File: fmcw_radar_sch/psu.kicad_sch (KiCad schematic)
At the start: 0 parts

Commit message: added MCU PSU VCO
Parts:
- added C1: 100nF, Capacitor_SMD:C_1206_3216Metric_Pad1.33x1.80mm_HandSolder, symbol Device:C_Small
- added C2: 10uF, Capacitor_SMD:C_1206_3216Metric_Pad1.33x1.80mm_HandSolder, symbol Device:C_Small
- added C203: 100n, Capacitor_SMD:C_0603_1608Metric, symbol Device:C
- added C205, C208: 1u, Capacitor_SMD:C_0805_2012Metric, symbol Device:C
- added C212, C215: 22u, Capacitor_SMD:C_0805_2012Metric, symbol Device:C
- added C3, C4: 22uF, Capacitor_SMD:C_1206_3216Metric_Pad1.33x1.80mm_HandSolder, symbol Device:C_Small
- added D204, D306, D307: Green, LED_SMD:LED_0603_1608Metric_Pad1.05x0.95mm_HandSolder, symbol Device:LED
- added J1: USB_B, Connector_USB:USB_B_OST_USB-B1HSxx_Horizontal, symbol Connector:USB_B
- added J2: Screw_Terminal_01x02, TerminalBlock:TerminalBlock_MaiXu_MX126-5.0-02P_1x02_P5.00mm, symbol Connector:Screw_Terminal_01x02
- added L1: 3.9uH, Inductor_SMD:L_Bourns_SDR0604, symbol Device:L_Small
- added L202: 10n, Inductor_SMD:L_APV_ANR6020, symbol Device:L
- added R1: 1k5, Resistor_SMD:R_1206_3216Metric_Pad1.30x1.75mm_HandSolder, symbol Device:R
- added R208, R301, R302: 1k, Resistor_SMD:R_0603_1608Metric_Pad0.98x0.95mm_HandSolder, symbol Device:R
- added SW1: SW_SPDT, Button_Switch_THT:SW_Slide_SPDT_Straight_CK_OS102011MS2Q, symbol Switch:SW_SPDT
- added U1: AP63203WU, Package_TO_SOT_SMD:TSOT-23-6, symbol Regulator_Switching:AP63203WU
- added U204: HT7533-1, Package_TO_SOT_SMD:SOT-89-3_Handsoldering, symbol Regulator_Linear:HT75xx-1-SOT89
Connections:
- new net: C2.1, C205.1, D307.2 (A), L202.1, SW1.2 (B), U1.2 (EN), U1.3 (IN)
- new net: D204.1 (K), R208.1
- new net: D306.1 (K), R301.1
- new net: C1.1, L1.1, U1.5 (SW)
- new net: C1.2, U1.6 (BST)
- new net: D307.1 (K), R302.1
- new net +3.3V: C3.2, C4.2, D306.2 (A), L1.2, R1.1, U1.1 (FB)
- new net +3.3VA: C215.1, D204.2 (A), U204.3 (VOUT)
- new net +BATT: J2.2 (Pin_2), SW1.1 (A)
- new net 5_volt_filt: C208.1, C212.1, L202.2, U204.2 (VIN)
- new net GND: C2.2, C203.1, C205.2, C208.2, C212.2, C215.2, C3.1, C4.1, J1.4 (GND), J2.1 (Pin_1), R208.2, R301.2, R302.2, U1.4 (GND), U204.1 (GND)
- new net USB_D+: J1.3 (D+), R1.2
- new net USB_D-: J1.2 (D-)
- new net VBUS: C203.2, J1.1 (VBUS), SW1.3 (C)
- no-connect marks 0 -> 1
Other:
- note added: "+BATT from screw Connector(nom. +9V)"
- note added: "3.3VA"
- note added: "Buck: 3.3V 2A"
- note added: "DCR=0R15"
- note added: "USB & POWER IN"
- note added: "VBUS from USB Connector(nom. +5V) Min. 22uF inp./outp. caps"

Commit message: board changes
board changes
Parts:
- added C23, C24: 1u, symbol Device:C_US
- added C25: 0.01u, symbol Device:C
- added C26: 10u, symbol Device:C
- added C27: C, symbol Device:C
- added D1, D2, D3: ESD131-B1-W0201, Diode_SMD:Infineon_SG-WLL-2-3_0.58x0.28_P0.36mm, symbol Diode:ESD131-B1-W0201
- added TP1, TP2: TestPoint, symbol Connector:TestPoint
- added U5: AP2112K-2.5, Package_TO_SOT_SMD:SOT-23-5, symbol Regulator_Linear:AP2112K-2.5
- added U6: LT1962-1.8, Package_SO:MSOP-8_3x3mm_P0.65mm, symbol Regulator_Linear:LT1962-1.8
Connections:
- net +3.3V: now also C23.1, C27.1, TP1.1, U5.1 (VIN), U5.3 (EN), U6.5 (~{SHDN}), U6.8 (IN)
- net +BATT: now also D3.2 (A2)
- net GND: now also C23.2, C24.2, C26.2, C27.2, D1.1 (A1), D2.1 (A1), D3.1 (A1), U5.2 (GND), U6.4 (GND)
- net USB_D+: now also D1.2 (A2)
- net USB_D-: now also D2.2 (A2)
- new net: C25.2, U6.3 (BYP)
- new net +1V8: C25.1, C26.1, U6.1 (OUT), U6.2 (SENSE)
- new net +2V5: C24.1, TP2.1, U5.5 (VOUT)
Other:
- note added: "+1.8V"
- note added: "+2.5V"
- moved on the sheet: C205, D307, J2, R302

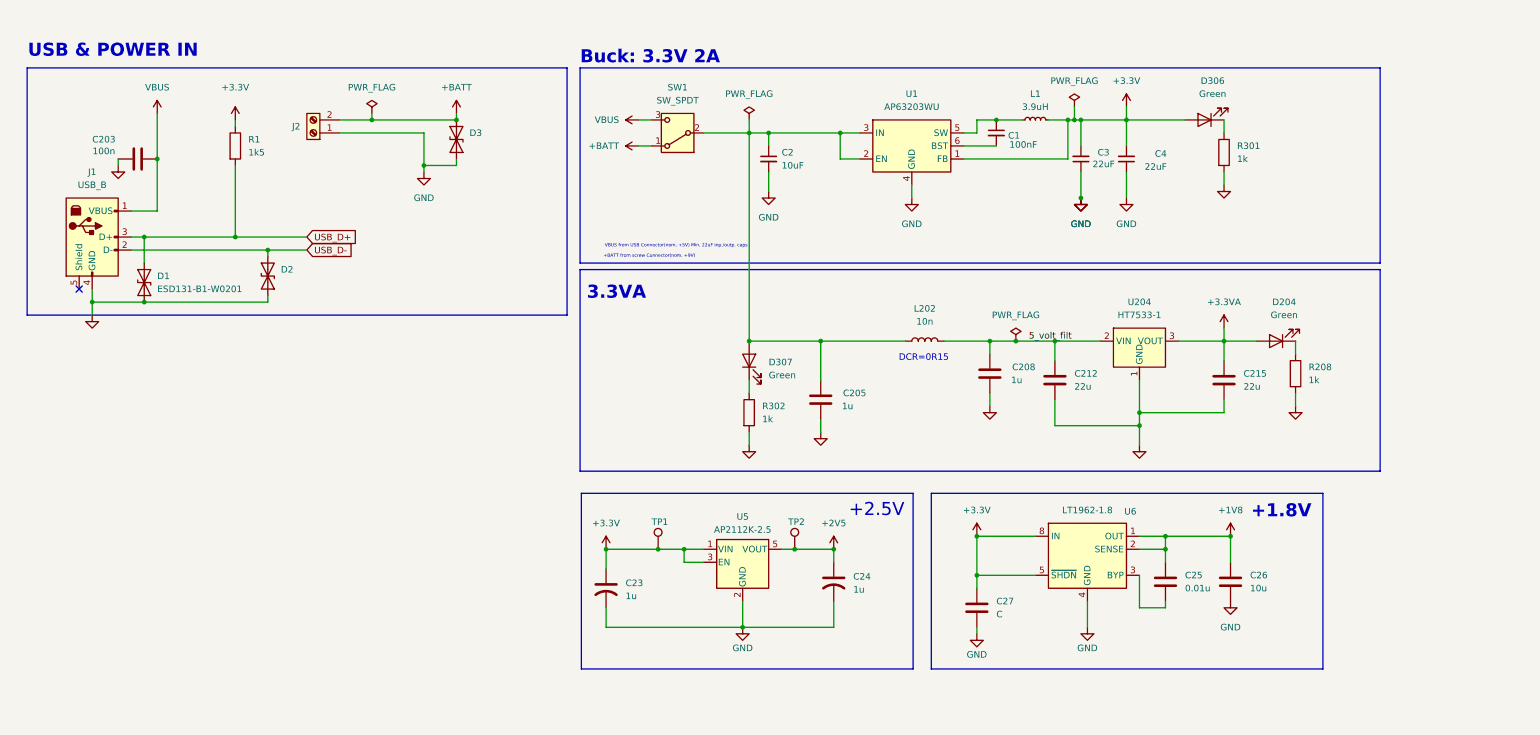
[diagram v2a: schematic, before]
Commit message: Layout of controller board
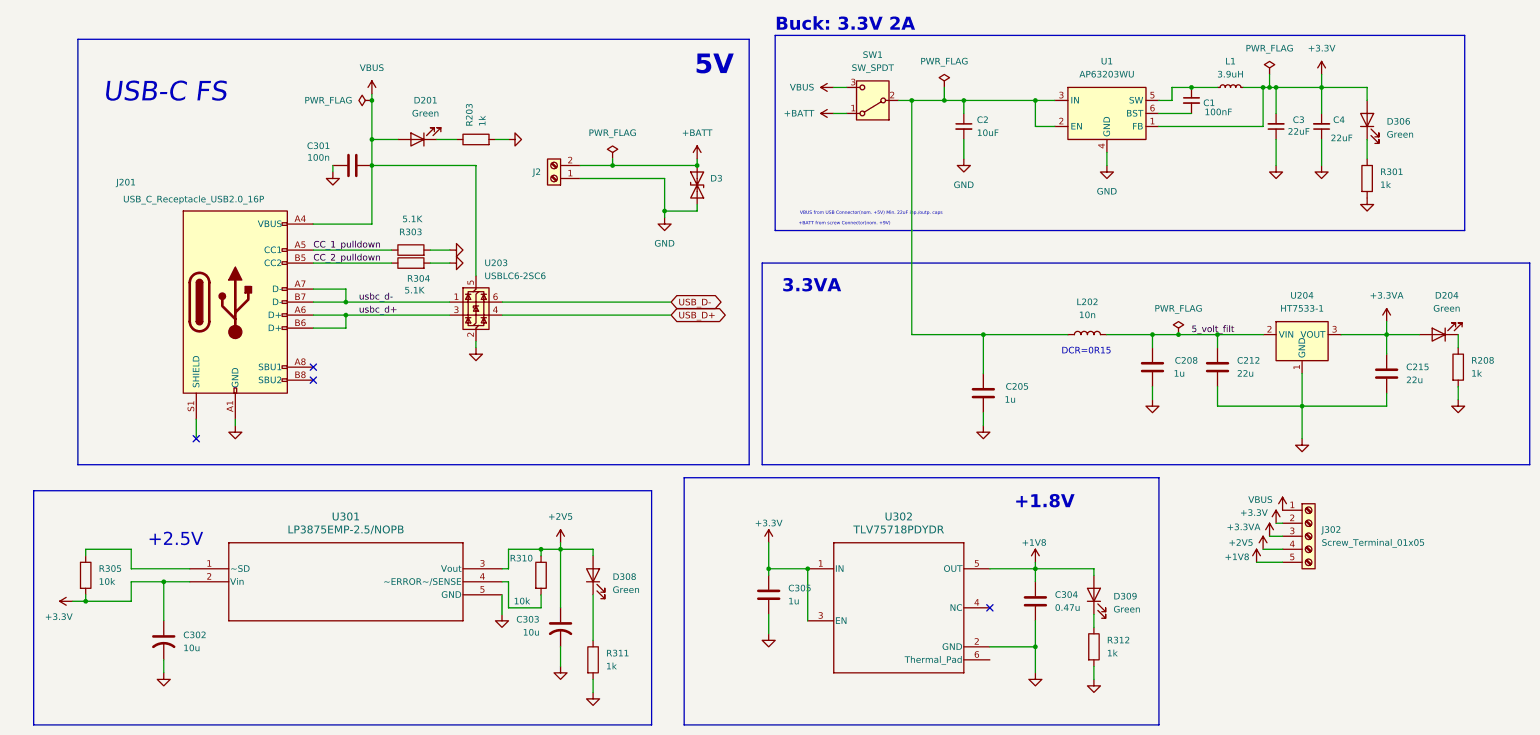
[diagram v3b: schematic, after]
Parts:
- removed C203: 100n, Capacitor_SMD:C_0603_1608Metric, symbol Device:C
- removed C23, C24: 1u, symbol Device:C_US
- removed C25: 0.01u, symbol Device:C
- removed C26: 10u, symbol Device:C
- removed C27: C, symbol Device:C
- removed D1, D2: ESD131-B1-W0201, Diode_SMD:Infineon_SG-WLL-2-3_0.58x0.28_P0.36mm, symbol Diode:ESD131-B1-W0201
- removed D307: Green, LED_SMD:LED_0603_1608Metric_Pad1.05x0.95mm_HandSolder, symbol Device:LED
- removed J1: USB_B, Connector_USB:USB_B_OST_USB-B1HSxx_Horizontal, symbol Connector:USB_B
- removed R1: 1k5, Resistor_SMD:R_1206_3216Metric_Pad1.30x1.75mm_HandSolder, symbol Device:R
- removed R302: 1k, Resistor_SMD:R_0603_1608Metric_Pad0.98x0.95mm_HandSolder, symbol Device:R
- removed TP1, TP2: TestPoint, symbol Connector:TestPoint
- removed U5: AP2112K-2.5, Package_TO_SOT_SMD:SOT-23-5, symbol Regulator_Linear:AP2112K-2.5
- removed U6: LT1962-1.8, Package_SO:MSOP-8_3x3mm_P0.65mm, symbol Regulator_Linear:LT1962-1.8
- added C301: 100n, Capacitor_SMD:C_0603_1608Metric, symbol Device:C
- added C302, C303: 10u, Capacitor_SMD:C_1206_3216Metric_Pad1.33x1.80mm_HandSolder, symbol Device:C_US
- added C304: 0.47u, Capacitor_SMD:C_1206_3216Metric_Pad1.33x1.80mm_HandSolder, symbol Device:C
- added C305: 1u, Capacitor_SMD:C_1206_3216Metric_Pad1.33x1.80mm_HandSolder, symbol Device:C
- added D201, D308, D309: Green, LED_SMD:LED_0603_1608Metric_Pad1.05x0.95mm_HandSolder, symbol Device:LED
- added J201: USB_C_Receptacle_USB2.0_16P, Connector_USB:USB_C_Receptacle_G-Switch_GT-USB-7010ASV, symbol Connector:USB_C_Receptacle_USB2.0_16P
- added J302: Screw_Terminal_01x05, TerminalBlock_Phoenix:TerminalBlock_Phoenix_MKDS-3-5-5.08_1x05_P5.08mm_Horizontal, symbol Connector:Screw_Terminal_01x05
- added R203, R311, R312: 1k, Resistor_SMD:R_0603_1608Metric_Pad0.98x0.95mm_HandSolder, symbol Device:R
- added R303, R304: 5.1K, Resistor_SMD:R_0603_1608Metric_Pad0.98x0.95mm_HandSolder, symbol Device:R
- added R305, R310: 10k, Resistor_SMD:R_1206_3216Metric_Pad1.30x1.75mm_HandSolder, symbol Device:R
- added U203: USBLC6-2SC6, Package_TO_SOT_SMD:SOT-23-6_Handsoldering, symbol Power_Protection:USBLC6-2SC6
- added U301: LP3875EMP-2.5/NOPB, nonkicad:MP05A, symbol non_kicad:LP3875EMP-2.5_NOPB
- added U302: TLV75718PDYDR, nonkicad:DYD0005A-MFG, symbol non_kicad:TLV75718PDYDR
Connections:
- net +1V8: now also C304.1, D309.2 (A), J302.5 (Pin_5), U302.5 (OUT)
- net +2V5: now also C303.1, D308.2 (A), J302.4 (Pin_4), R310.1, U301.3 (Vout)
- net +3.3V: now also C302.1, C305.1, J302.2 (Pin_2), R305.2, U301.2 (Vin), U302.1 (IN), U302.3 (EN)
- net +3.3VA: now also J302.3 (Pin_3)
- net GND: now also C301.1, C302.2, C303.2, C304.2, C305.2, J201.A1 (GND), J201.A12 (GND), J201.B1 (GND), J201.B12 (GND), R203.2, R303.2, R304.2, R311.2, R312.2, U203.2 (GND), U301.5 (GND), U302.2 (GND)
- net USB_D+: now also U203.4 (I/O2)
- net USB_D-: now also U203.6 (I/O1)
- net VBUS: now also C301.2, D201.2 (A), J201.A4 (VBUS), J201.A9 (VBUS), J201.B4 (VBUS), J201.B9 (VBUS), J302.1 (Pin_1), U203.5 (VBUS)
- new net: R310.2, U301.4 (~ERROR~/SENSE)
- new net: D201.1 (K), R203.1
- new net: D308.1 (K), R311.1
- new net: R305.1, U301.1 (~SD)
- new net: D309.1 (K), R312.1
- new net CC_1_pulldown: J201.A5 (CC1), R303.1
- new net CC_2_pulldown: J201.B5 (CC2), R304.1
- new net usbc_d+: J201.A6 (D+), J201.B6 (D+), U203.3 (I/O2)
- new net usbc_d-: J201.A7 (D-), J201.B7 (D-), U203.1 (I/O1)
- no-connect marks 1 -> 4
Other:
- note added: "5V"
- note added: "USB-C FS"
- note removed: "USB & POWER IN"
- moved on the sheet: C1, C2, C205, C208, C212, C215, C3, C4, D204, D3, D306, J2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

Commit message: CHANGES
changes
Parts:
- renumbered C302 to C12, C301 to C13, C303 to C14, C305 to C15, C2 to C16, C205 to C17, C304 to C18, C208 to C19, C1 to C20, C212 to C21, C3 to C22, C4 to C23, C215 to C24, D201 to D2, D308 to D3, D3 to D4, D309 to D5, D306 to D6, D204 to D7, J302 to J10, J201 to J8, J2 to J9, L202 to L2, L1 to L3, R303 to R10, R304 to R11, R203 to R12, R310 to R13, R311 to R14, R312 to R15, R301 to R16, R208 to R17, R305 to R9, SW1 to SW2, U301 to U2, U203 to U3, U302 to U4, U1 to U5, U204 to U6
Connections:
- net SW: now reaches C20.1, L3.1, U5.5 (SW)
- net BST: now reaches C20.2, U5.6 (BST)

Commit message: Routing
Routing
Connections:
- net V_PREfilt: now reaches C16.1, C17.1, L2.1, SW2.2 (B), U5.2 (EN), U5.3 (IN)
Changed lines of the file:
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@@
 	)
 	(label "SW"
-		(at 238.76 30.48 0)
+		(at 237.49 30.48 0)
 		(effects
 			(font
@@
 		(effects
 			(font
+				(size 1.27 1.27)
+			)
+			(justify left bottom)
+		)
+	)
+	(label "V_PREfilt"
+		(at 198.12 78.74 0)
+		(effects
+			(font
